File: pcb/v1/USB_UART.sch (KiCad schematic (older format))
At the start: 1 part

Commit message: Finish the schematic
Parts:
- added C13: 10uF, Capacitor_THT:C_Disc_D3.8mm_W2.6mm_P2.50mm, symbol Device:C
- added C14, C15: 0.1uF, Capacitor_THT:C_Disc_D3.8mm_W2.6mm_P2.50mm, symbol Device:C
- added D3: TX, LED_THT:LED_D5.0mm, symbol Device:LED
- added D4: RX, LED_THT:LED_D5.0mm, symbol Device:LED
- added J4: USB_B_Mini, Connector_USB:USB_Mini-B_Lumberg_2486_01_Horizontal, symbol Connector:USB_B_Mini
- added JP1: USBPWR, Connector_PinHeader_2.54mm:PinHeader_1x02_P2.54mm_Vertical, symbol Device:Jumper_NC_Small
- added R12, R13: 1K, Resistor_THT:R_Axial_DIN0207_L6.3mm_D2.5mm_P10.16mm_Horizontal, symbol Device:R
- gave numbers to parts that had none: 1
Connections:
- net GND: now also U10.26 (TEST), C13.2, C14.2, C15.1, J4.5 (GND), J4.6 (Shield)
- net RX: now also U10.1 (TXD); no longer U10.5 (RXD)
- net TX: now also U10.5 (RXD); no longer U10.1 (TXD)
- net VCC: now also C13.1, C14.1, JP1.2, R12.1, R13.1
- net ~RTS: now reaches U10.11 (CTS)
- net at U10.15 (USBD+): now also J4.3 (D+)
- net at U10.16 (USBD-): now also J4.2 (D-)
- net at U10.17 (3V3OUT): now also C15.2
- net at U10.22 (CBUS1): now also D4.1 (K)
- net at U10.23 (CBUS0): now also D3.1 (K)
- new net: J4.1 (VBUS), JP1.1
- new net: D3.2 (A), R12.2
- new net: D4.2 (A), R13.2
- no-connect marks 0 -> 12
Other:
- moved on the sheet: U10

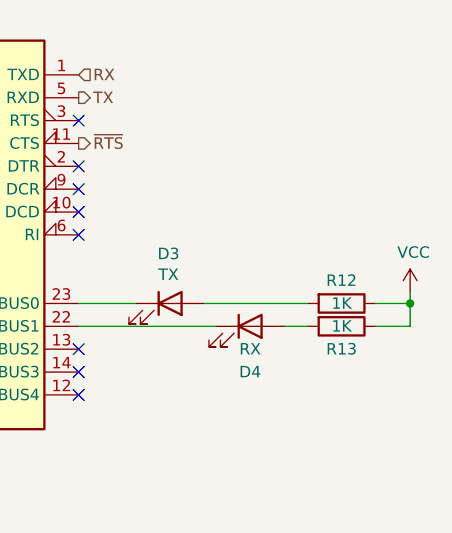
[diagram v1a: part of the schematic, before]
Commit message: Place components on the PCB layout
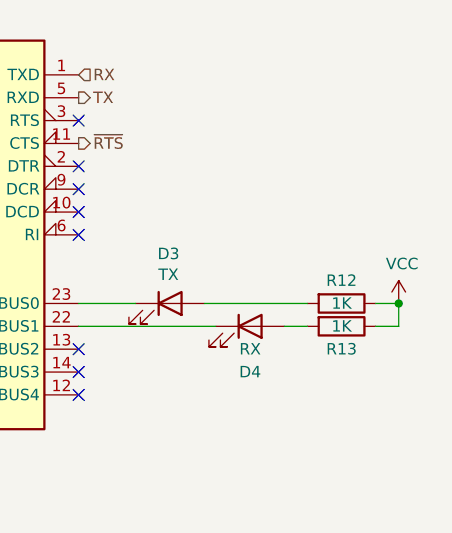
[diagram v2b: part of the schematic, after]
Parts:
- R12, R13: footprint Resistor_THT:R_Axial_DIN0207_L6.3mm_D2.5mm_P10.16mm_Horizontal -> (none)
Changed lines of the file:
@@
 Wire Wire Line
 	7500 3750 7750 3750
-$Comp
-L Device:R R12
-U 1 1 5FF7C0ED
-P 8650 3750
-F 0 "R12" V 8550 3750 50  0000 C CNN
-F 1 "1K" V 8650 3750 50  0000 C CNN
-F 2 "Resistor_THT:R_Axial_DIN0207_L6.3mm_D2.5mm_P10.16mm_Horizontal" V 8580 3750 50  0001 C CNN
-F 3 "~" H 8650 3750 50  0001 C CNN
-	1    8650 3750
-	0    1    1    0
-$EndComp
-$Comp
-L Device:R R13
-U 1 1 5FF7C707
-P 8650 3850
-F 0 "R13" V 8750 3850 50  0000 C CNN
-F 1 "1K" V 8650 3850 50  0000 C CNN
-F 2 "Resistor_THT:R_Axial_DIN0207_L6.3mm_D2.5mm_P10.16mm_Horizontal" V 8580 3850 50  0001 C CNN
-F 3 "~" H 8650 3850 50  0001 C CNN
-	1    8650 3850
-	0    1    1    0
-$EndComp
 Wire Wire Line
 	8050 3750 8500 3750
 Wire Wire Line
 	8400 3850 8500 3850
-$Comp
-L power:VCC #PWR068
-U 1 1 5FF7DED7
-P 8950 3700
-F 0 "#PWR068" H 8950 3550 50  0001 C CNN
-F 1 "VCC" H 8965 3873 50  0000 C CNN
-F 2 "" H 8950 3700 50  0001 C CNN
-F 3 "" H 8950 3700 50  0001 C CNN
-	1    8950 3700
-	1    0    0    -1
-$EndComp
-Wire Wire Line
-	8950 3700 8950 3750
-Wire Wire Line
-	8950 3850 8800 3850
-Wire Wire Line
-	8800 3750 8950 3750
-Connection ~ 8950 3750
-Wire Wire Line
-	8950 3750 8950 3850
 NoConn ~ 5900 3450
 $Comp
@@
 	1    0    0    -1
 $EndComp
+$Comp
+L Device:R R12
+U 1 1 6016C208
+P 8650 3750
+F 0 "R12" V 8550 3750 50  0000 C CNN
+F 1 "1K" V 8650 3750 50  0000 C CNN
+F 2 "" V 8580 3750 50  0001 C CNN
+F 3 "~" H 8650 3750 50  0001 C CNN
+	1    8650 3750
+	0    1    1    0
+$EndComp
+$Comp
+L Device:R R13
+U 1 1 6016C676
+P 8650 3850
+F 0 "R13" V 8750 3850 50  0000 C CNN
+F 1 "1K" V 8650 3850 50  0000 C CNN
+F 2 "" V 8580 3850 50  0001 C CNN
+F 3 "~" H 8650 3850 50  0001 C CNN
+	1    8650 3850
+	0    1    1    0
+$EndComp
+$Comp
+L power:VCC #PWR0106
+U 1 1 6016CBA6
+P 8900 3750
+F 0 "#PWR0106" H 8900 3600 50  0001 C CNN
+F 1 "VCC" H 8915 3923 50  0000 C CNN
+F 2 "" H 8900 3750 50  0001 C CNN
+F 3 "" H 8900 3750 50  0001 C CNN
+	1    8900 3750
+	1    0    0    -1
+$EndComp
+Wire Wire Line
+	8800 3750 8900 3750
+Wire Wire Line
+	8800 3850 8900 3850
+Wire Wire Line
+	8900 3850 8900 3750
+Connection ~ 8900 3750
 $EndSCHEMATC

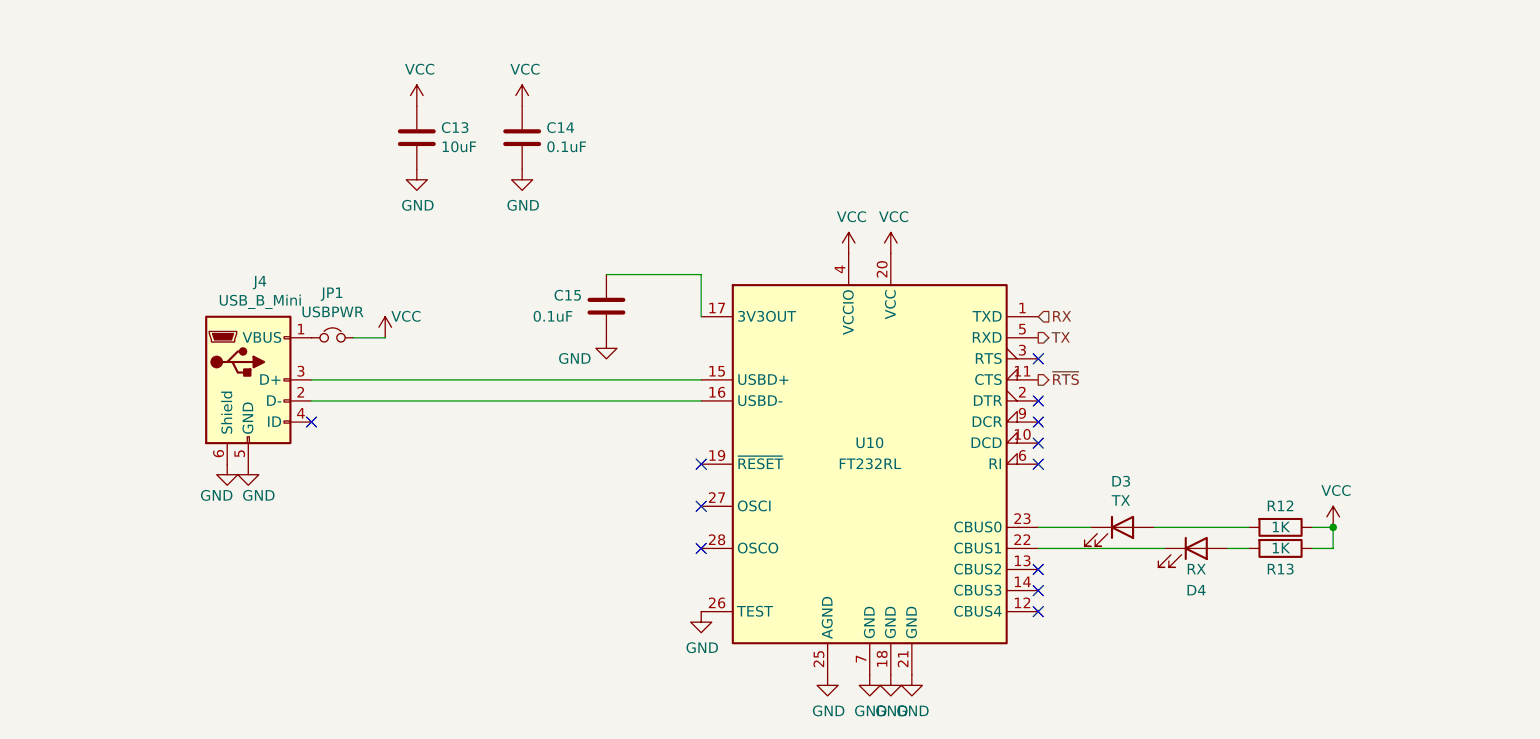
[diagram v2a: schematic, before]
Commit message: Finish PCB layout
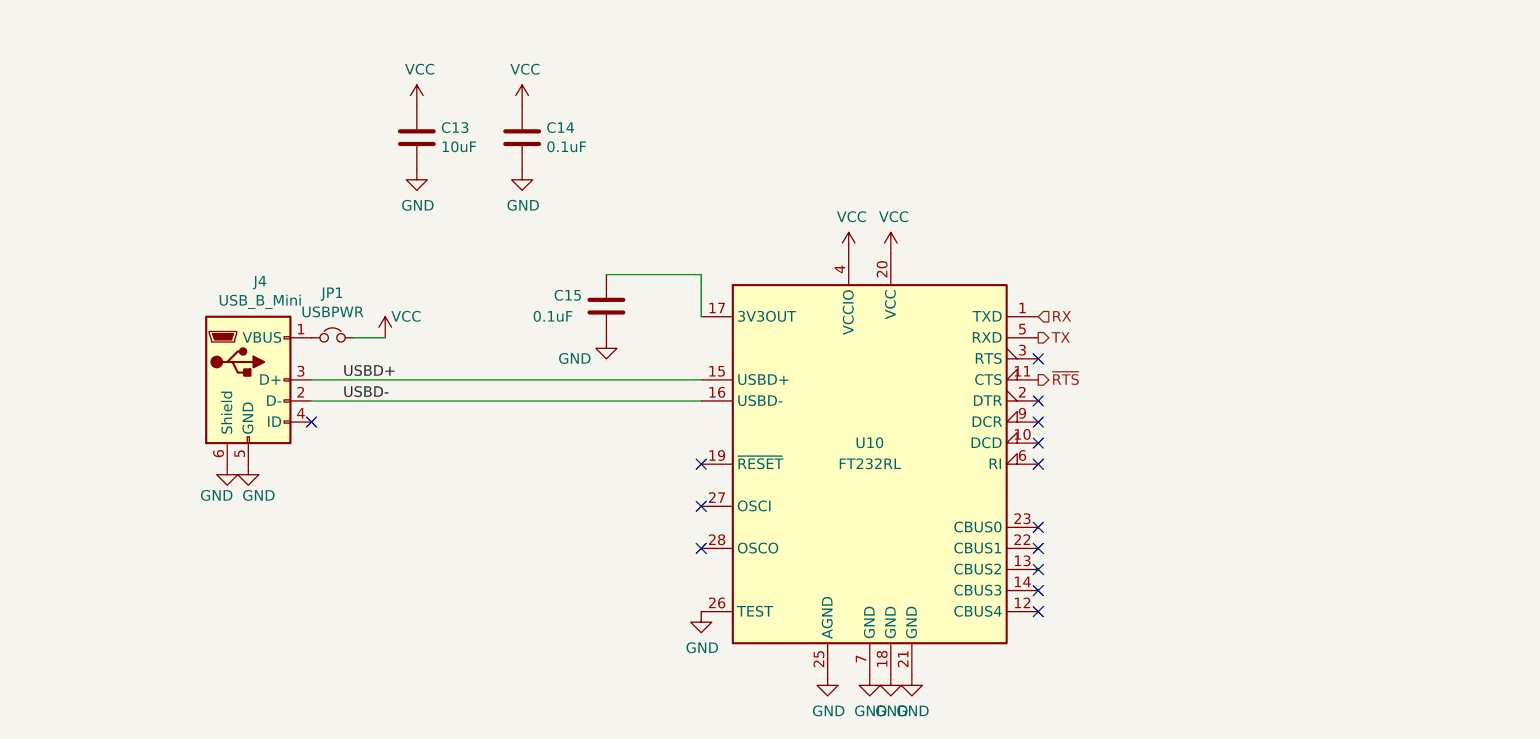
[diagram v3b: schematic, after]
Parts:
- removed D3: TX, LED_THT:LED_D5.0mm, symbol Device:LED
- removed D4: RX, LED_THT:LED_D5.0mm, symbol Device:LED
- removed R12, R13: 1K, symbol Device:R
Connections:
- net USBD-: now reaches J4.2 (D-), U10.16 (USBD-)
- net USBD+: now reaches J4.3 (D+), U10.15 (USBD+)
- no-connect marks 12 -> 14
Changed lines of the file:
@@
 NoConn ~ 7500 3350
 NoConn ~ 7500 3150
-$Comp
-L Device:LED D3
-U 1 1 5FF7AB93
-P 7900 3750
-F 0 "D3" H 7893 3967 50  0000 C CNN
-F 1 "TX" H 7893 3876 50  0000 C CNN
-F 2 "LED_THT:LED_D5.0mm" H 7900 3750 50  0001 C CNN
-F 3 "~" H 7900 3750 50  0001 C CNN
-	1    7900 3750
-	1    0    0    -1
-$EndComp
-$Comp
-L Device:LED D4
-U 1 1 5FF7B1AA
-P 8250 3850
-F 0 "D4" H 8250 3650 50  0000 C CNN
-F 1 "RX" H 8250 3750 50  0000 C CNN
-F 2 "LED_THT:LED_D5.0mm" H 8250 3850 50  0001 C CNN
-F 3 "~" H 8250 3850 50  0001 C CNN
-	1    8250 3850
-	1    0    0    -1
-$EndComp
-Wire Wire Line
-	7500 3850 8100 3850
-Wire Wire Line
-	7500 3750 7750 3750
-Wire Wire Line
-	8050 3750 8500 3750
-Wire Wire Line
-	8400 3850 8500 3850
 NoConn ~ 5900 3450
 $Comp
@@
 	1    0    0    -1
 $EndComp
-$Comp
-L Device:R R12
-U 1 1 6016C208
-P 8650 3750
-F 0 "R12" V 8550 3750 50  0000 C CNN
-F 1 "1K" V 8650 3750 50  0000 C CNN
-F 2 "" V 8580 3750 50  0001 C CNN
-F 3 "~" H 8650 3750 50  0001 C CNN
-	1    8650 3750
-	0    1    1    0
-$EndComp
-$Comp
-L Device:R R13
-U 1 1 6016C676
-P 8650 3850
-F 0 "R13" V 8750 3850 50  0000 C CNN
-F 1 "1K" V 8650 3850 50  0000 C CNN
-F 2 "" V 8580 3850 50  0001 C CNN
-F 3 "~" H 8650 3850 50  0001 C CNN
-	1    8650 3850
-	0    1    1    0
-$EndComp
-$Comp
-L power:VCC #PWR0106
-U 1 1 6016CBA6
-P 8900 3750
-F 0 "#PWR0106" H 8900 3600 50  0001 C CNN
-F 1 "VCC" H 8915 3923 50  0000 C CNN
-F 2 "" H 8900 3750 50  0001 C CNN
-F 3 "" H 8900 3750 50  0001 C CNN
-	1    8900 3750
-	1    0    0    -1
-$EndComp
-Wire Wire Line
-	8800 3750 8900 3750
-Wire Wire Line
-	8800 3850 8900 3850
-Wire Wire Line
-	8900 3850 8900 3750
-Connection ~ 8900 3750
+NoConn ~ 7500 3750
+NoConn ~ 7500 3850
+Text Label 4200 3050 0    50   ~ 0
+USBD+
+Text Label 4200 3150 0    50   ~ 0
+USBD-
 $EndSCHEMATC

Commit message: Add UART socket and other PCB improvements
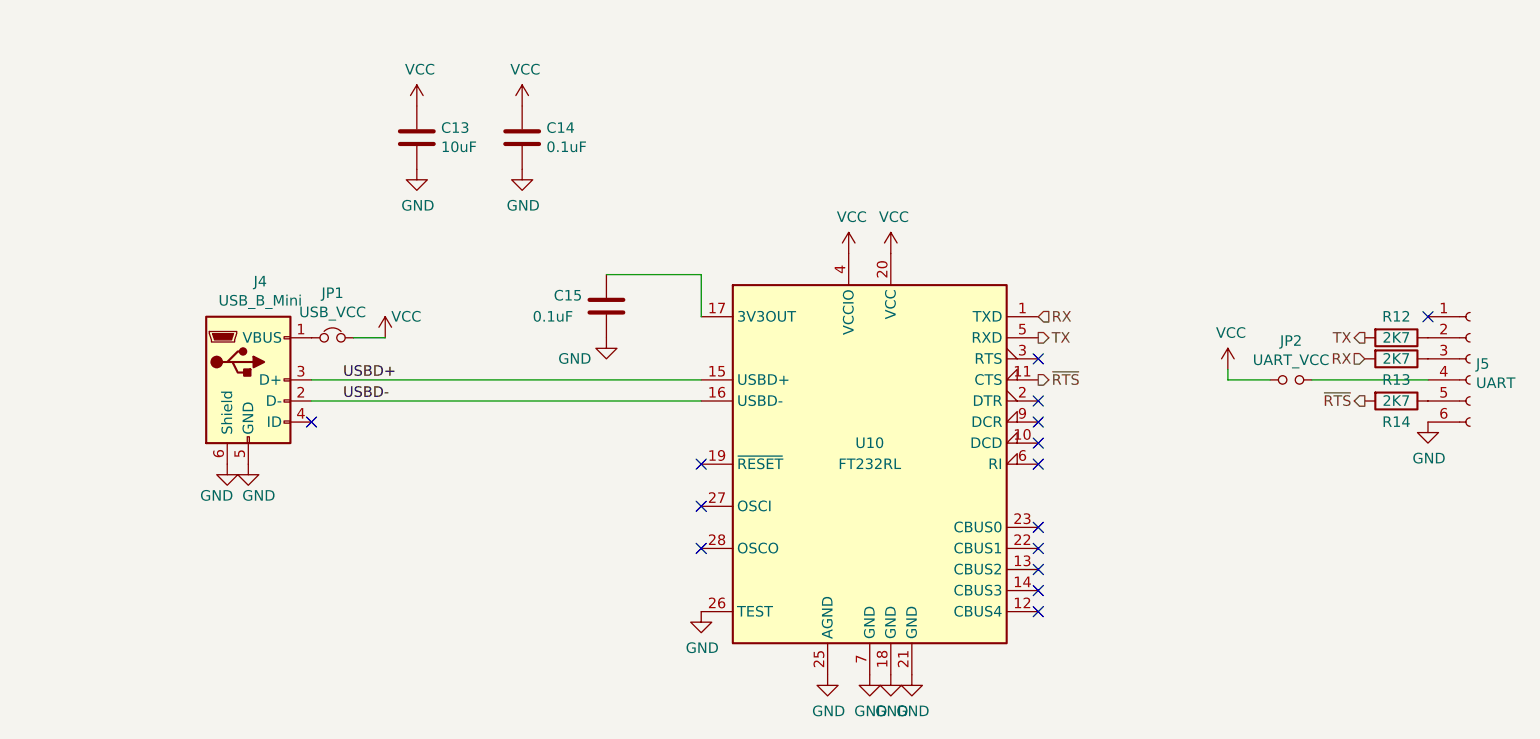
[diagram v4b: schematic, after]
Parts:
- added J5: UART, Connector_PinHeader_2.54mm:PinHeader_1x06_P2.54mm_Vertical, symbol Connector:Conn_01x06_Female
- added JP2: UART_VCC, Connector_PinHeader_2.54mm:PinHeader_1x02_P2.54mm_Vertical, symbol Device:Jumper_NO_Small
- added R12, R13, R14: 2K7, Resistor_THT:R_Axial_DIN0207_L6.3mm_D2.5mm_P10.16mm_Horizontal, symbol Device:R
- JP1: value USBPWR -> USB_VCC
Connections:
- net GND: now also J5.6 (Pin_6)
- net RX: now also R13.2
- net TX: now also R12.2
- net VCC: now also JP2.1
- net ~RTS: now also R14.2
- new net: J5.2 (Pin_2), R12.1
- new net: J5.3 (Pin_3), R13.1
- new net: J5.4 (Pin_4), JP2.2
- new net: J5.5 (Pin_5), R14.1
- no-connect marks 14 -> 15
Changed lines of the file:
@@
 P 4150 2850
 F 0 "JP1" H 4150 3062 50  0000 C CNN
-F 1 "USBPWR" H 4150 2971 50  0000 C CNN
+F 1 "USB_VCC" H 4150 2971 50  0000 C CNN
 F 2 "Connector_PinHeader_2.54mm:PinHeader_1x02_P2.54mm_Vertical" H 4150 2850 50  0001 C CNN
 F 3 "~" H 4150 2850 50  0001 C CNN
@@
 Text Label 4200 3150 0    50   ~ 0
 USBD-
+$Comp
+L Connector:Conn_01x06_Female J5
+U 1 1 60B8677D
+P 9550 2950
+F 0 "J5" H 9578 2926 50  0000 L CNN
+F 1 "UART" H 9578 2835 50  0000 L CNN
+F 2 "Connector_PinHeader_2.54mm:PinHeader_1x06_P2.54mm_Vertical" H 9550 2950 50  0001 C CNN
+F 3 "~" H 9550 2950 50  0001 C CNN
+	1    9550 2950
+	1    0    0    -1
+$EndComp
+$Comp
+L Device:R R12
+U 1 1 60B8780A
+P 9200 2850
+F 0 "R12" V 9100 2850 50  0000 C CNN
+F 1 "2K7" V 9200 2850 50  0000 C CNN
+F 2 "Resistor_THT:R_Axial_DIN0207_L6.3mm_D2.5mm_P10.16mm_Horizontal" V 9130 2850 50  0001 C CNN
+F 3 "~" H 9200 2850 50  0001 C CNN
+	1    9200 2850
+	0    1    1    0
+$EndComp
+NoConn ~ 9350 2750
+$Comp
+L Device:R R13
+U 1 1 60B8845F
+P 9200 2950
+F 0 "R13" V 9300 2950 50  0000 C CNN
+F 1 "2K7" V 9200 2950 50  0000 C CNN
+F 2 "Resistor_THT:R_Axial_DIN0207_L6.3mm_D2.5mm_P10.16mm_Horizontal" V 9130 2950 50  0001 C CNN
+F 3 "~" H 9200 2950 50  0001 C CNN
+	1    9200 2950
+	0    1    1    0
+$EndComp
+Text HLabel 9050 2950 0    50   Input ~ 0
+RX
+Text HLabel 9050 2850 0    50   Output ~ 0
+TX
+$Comp
+L Device:Jumper_NO_Small JP2
+U 1 1 60B88B00
+P 8700 3050
+F 0 "JP2" H 8700 3235 50  0000 C CNN
+F 1 "UART_VCC" H 8700 3144 50  0000 C CNN
+F 2 "Connector_PinHeader_2.54mm:PinHeader_1x02_P2.54mm_Vertical" H 8700 3050 50  0001 C CNN
+F 3 "~" H 8700 3050 50  0001 C CNN
+	1    8700 3050
+	1    0    0    -1
+$EndComp
+Wire Wire Line
+	8800 3050 9350 3050
+$Comp
+L power:VCC #PWR049
+U 1 1 60B8B1B0
+P 8400 3000
+F 0 "#PWR049" H 8400 2850 50  0001 C CNN
+F 1 "VCC" H 8415 3173 50  0000 C CNN
+F 2 "" H 8400 3000 50  0001 C CNN
+F 3 "" H 8400 3000 50  0001 C CNN
+	1    8400 3000
+	1    0    0    -1
+$EndComp
+Wire Wire Line
+	8400 3000 8400 3050
+Wire Wire Line
+	8400 3050 8600 3050
+$Comp
+L Device:R R14
+U 1 1 60B8BFD6
+P 9200 3150
+F 0 "R14" V 9300 3150 50  0000 C CNN
+F 1 "2K7" V 9200 3150 50  0000 C CNN
+F 2 "Resistor_THT:R_Axial_DIN0207_L6.3mm_D2.5mm_P10.16mm_Horizontal" V 9130 3150 50  0001 C CNN
+F 3 "~" H 9200 3150 50  0001 C CNN
+	1    9200 3150
+	0    1    1    0
+$EndComp
+Text HLabel 9050 3150 0    50   Output ~ 0
+~RTS
+$Comp
+L power:GND #PWR068
+U 1 1 60B8C642
+P 9350 3250
+F 0 "#PWR068" H 9350 3000 50  0001 C CNN
+F 1 "GND" H 9355 3077 50  0000 C CNN
+F 2 "" H 9350 3250 50  0001 C CNN
+F 3 "" H 9350 3250 50  0001 C CNN
+	1    9350 3250
+	1    0    0    -1
+$EndComp
 $EndSCHEMATC

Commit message: Noop
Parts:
- J4: symbol Connector:USB_B_Mini -> hobgoblin_v1-rescue:USB_B_Mini-Connector
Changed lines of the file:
@@
 TX
 $Comp
-L Connector:USB_B_Mini J4
+L hobgoblin_v1-rescue:USB_B_Mini-Connector J4
 U 1 1 5FAD533D
 P 3750 3050

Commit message: Fix CF footprint pin numbering
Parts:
- C13: footprint Capacitor_THT:C_Disc_D3.8mm_W2.6mm_P2.50mm -> Capacitor_THT:CP_Radial_D4.0mm_P1.50mm
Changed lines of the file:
@@
 F 0 "C13" H 4665 1946 50  0000 L CNN
 F 1 "10uF" H 4665 1855 50  0000 L CNN
-F 2 "Capacitor_THT:C_Disc_D3.8mm_W2.6mm_P2.50mm" H 4588 1750 50  0001 C CNN
+F 2 "Capacitor_THT:CP_Radial_D4.0mm_P1.50mm" H 4588 1750 50  0001 C CNN
 F 3 "~" H 4550 1900 50  0001 C CNN
 	1    4550 1900
